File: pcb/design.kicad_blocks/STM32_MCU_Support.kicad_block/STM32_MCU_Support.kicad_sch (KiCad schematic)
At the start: 11 parts

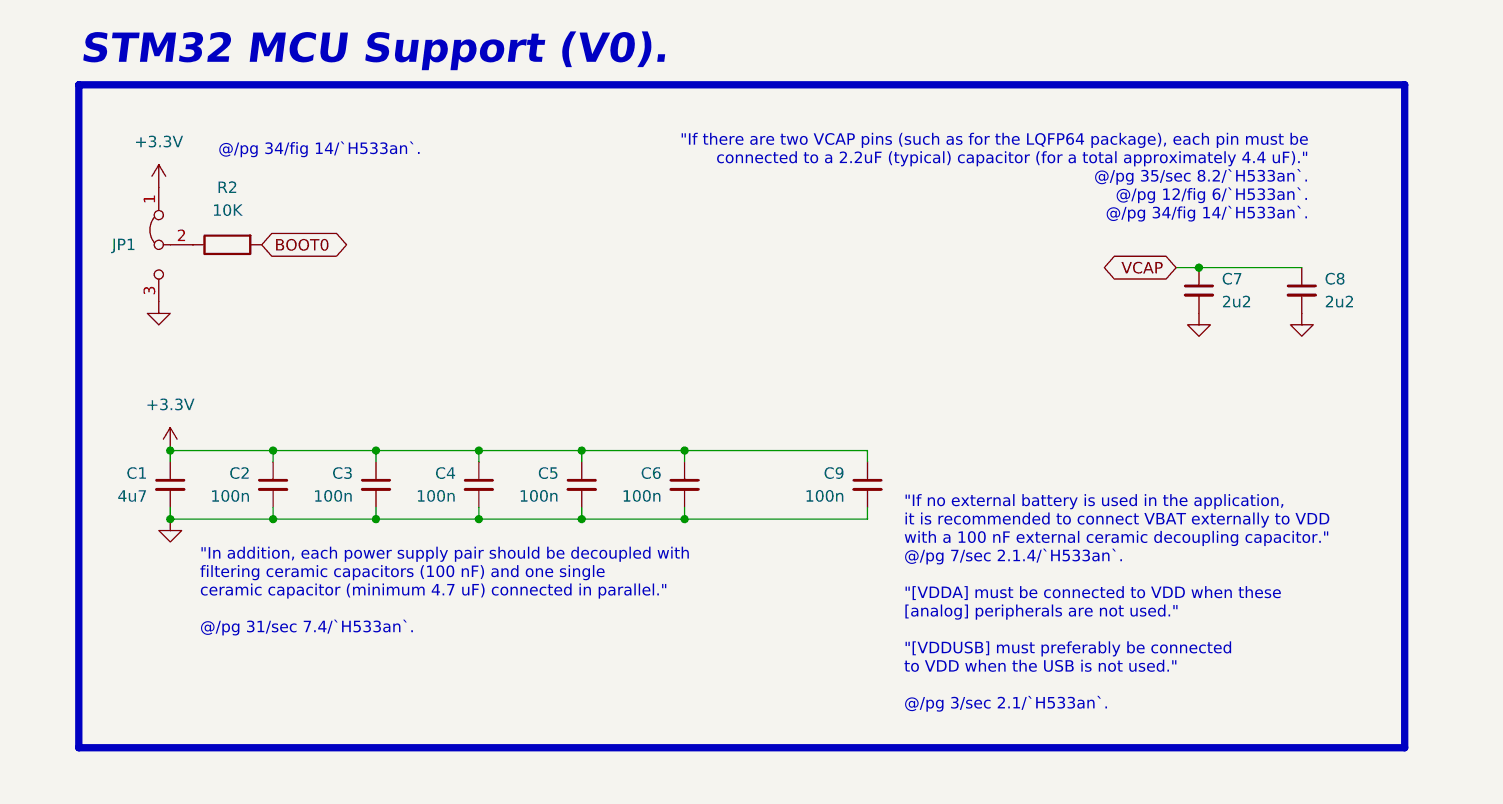
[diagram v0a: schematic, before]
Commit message: `STM32 MCU Support (V1 : Smaller BOOT0 setting).`
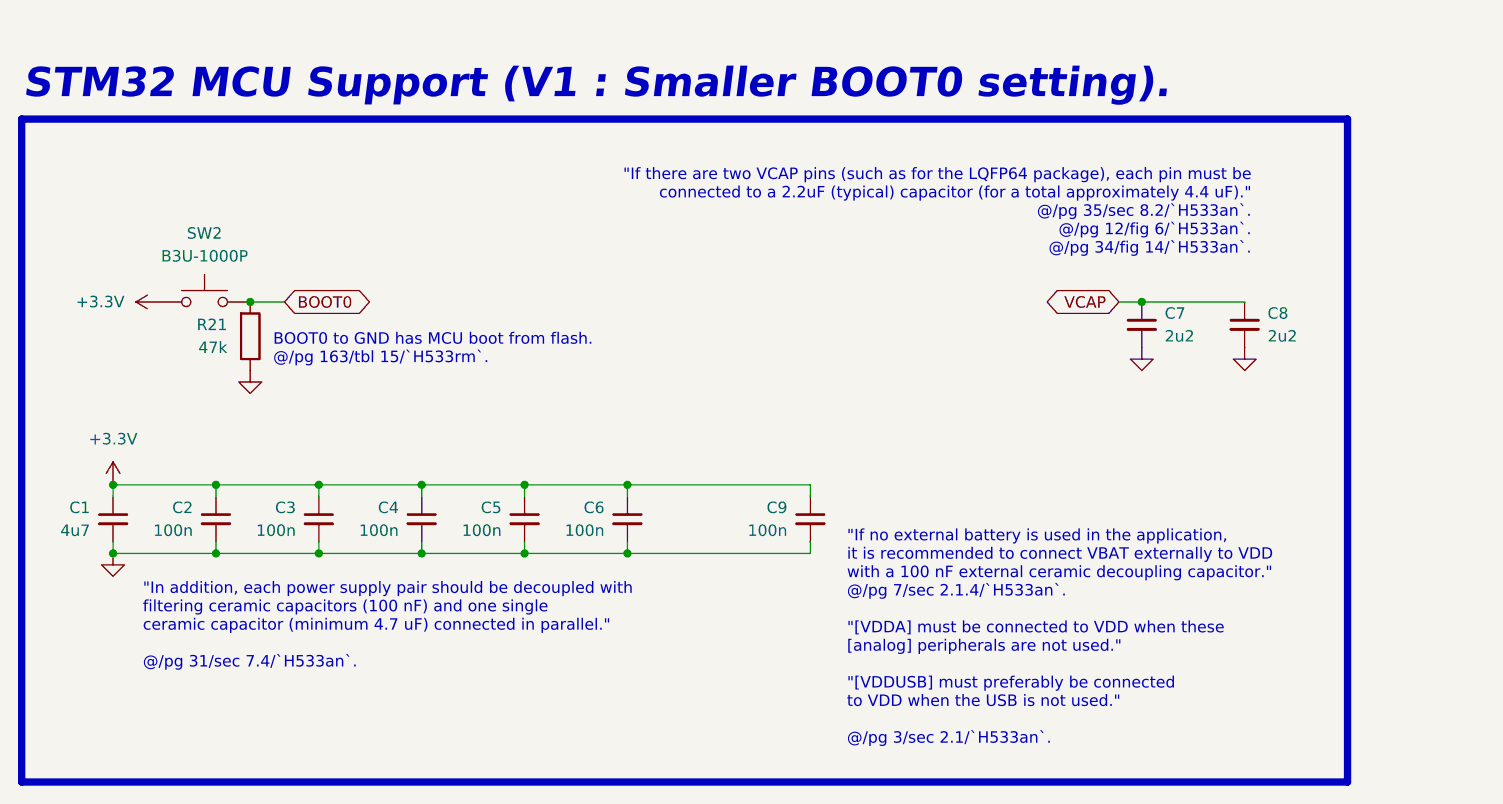
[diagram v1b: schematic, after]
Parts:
- removed JP1: Jumper_3_Bridged12, Connector_PinHeader_2.54mm:PinHeader_1x03_P2.54mm_Vertical, symbol Jumper:Jumper_3_Bridged12
- removed R2: 10K, Resistor_SMD:R_1206_3216Metric_Pad1.30x1.75mm_HandSolder, symbol Device:R
- added R21: 47k, Resistor_SMD:R_1206_3216Metric_Pad1.30x1.75mm_HandSolder, symbol Device:R
- added SW2: B3U-1000P, Button_Switch_SMD:SW_SPST_B3U-1000P, symbol Switch:SW_Push
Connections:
- net +3.3V: now also SW2.1
- net BOOT0: now also R21.2, SW2.2
- net GND: now also R21.1
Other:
- note added: "BOOT0 to GND has MCU boot from flash. @/pg 163/tbl 15/`H533rm`."
- note added: "STM32 MCU Support (V1 : Smaller BOOT0 setting)."
- note removed: "@/pg 34/fig 14/`H533an`."
- note removed: "STM32 MCU Support (V0)."
- moved on the sheet: C1, C2, C3, C4, C5, C6, C7, C8, C9
